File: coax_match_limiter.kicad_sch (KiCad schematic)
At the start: 10 parts, among them J1 BNC, J2 limiter

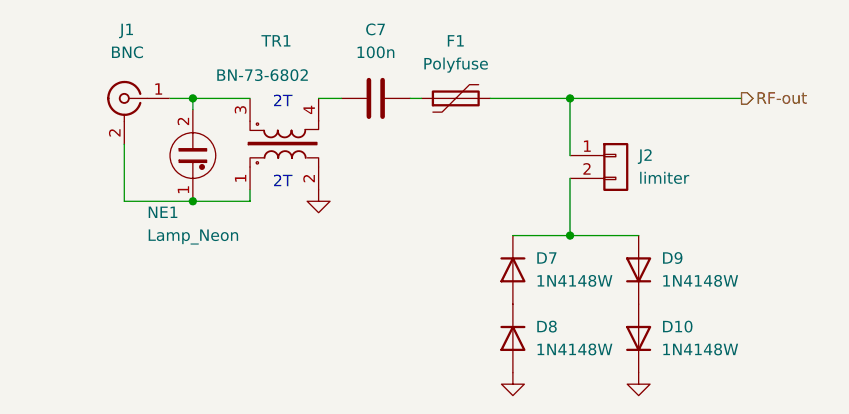
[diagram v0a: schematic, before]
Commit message: added BNC part number
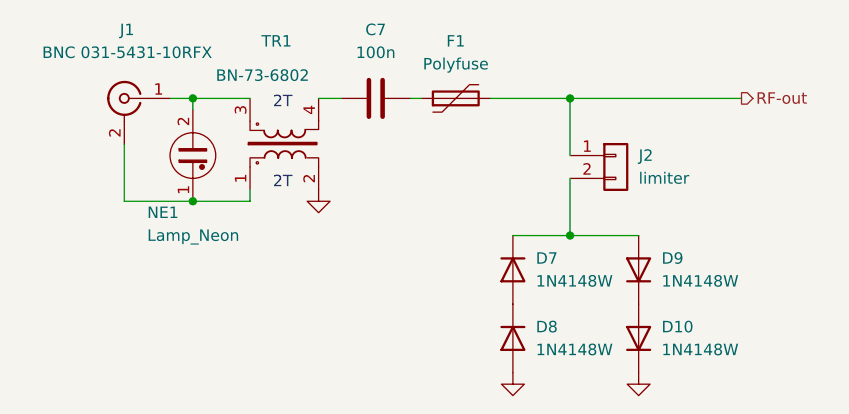
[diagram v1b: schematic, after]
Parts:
- J1: value BNC -> BNC 031-5431-10RFX
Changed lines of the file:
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@@
     (in_bom yes) (on_board yes) (fields_autoplaced)
     (property "Reference" "J1" (id 0) (at 72.7074 72.39 0))
-    (property "Value" "BNC" (id 1) (at 72.7074 74.93 0))
+    (property "Value" "BNC 031-5431-10RFX" (id 1) (at 72.7074 74.93 0))
     (property "Footprint" "Components:BNC_horizontal" (id 2) (at 72.39 80.01 0)
       (effects (font (size 1.27 1.27)) hide)

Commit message: update CMM footprint and board name
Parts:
- TR1: footprint Components:BN-73-6802-balun -> Components:BN-73-6802-2-0
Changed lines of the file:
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@@
       (effects (font (size 1.27 1.27)) (justify right))
     )
-    (property "Footprint" "Components:BN-73-6802-balun" (id 2) (at 99.06 85.09 0)
+    (property "Footprint" "Components:BN-73-6802-2-0" (id 2) (at 99.06 85.09 0)
       (effects (font (size 1.27 1.27) italic) hide)
     )
